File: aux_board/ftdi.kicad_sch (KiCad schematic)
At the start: 12 parts, among them U4 FT230XS

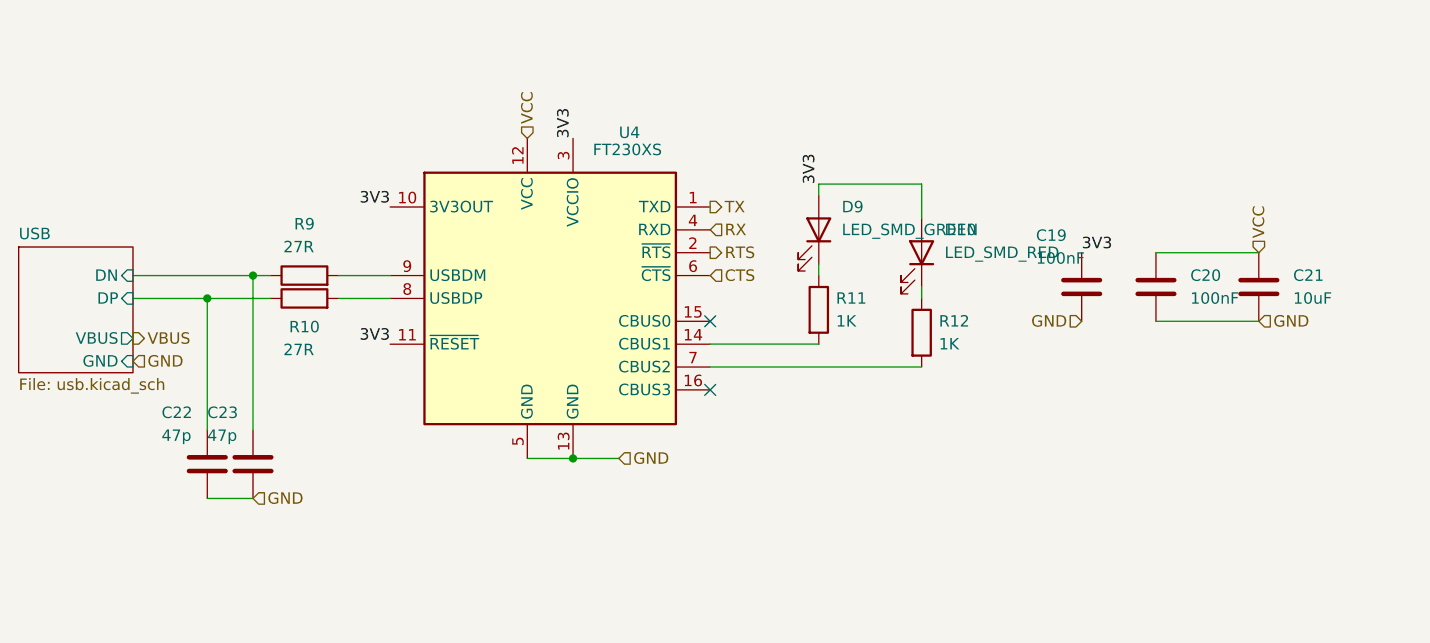
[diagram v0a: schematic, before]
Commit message: tweaking SCI and AUX for production, using common sheets as much as possible
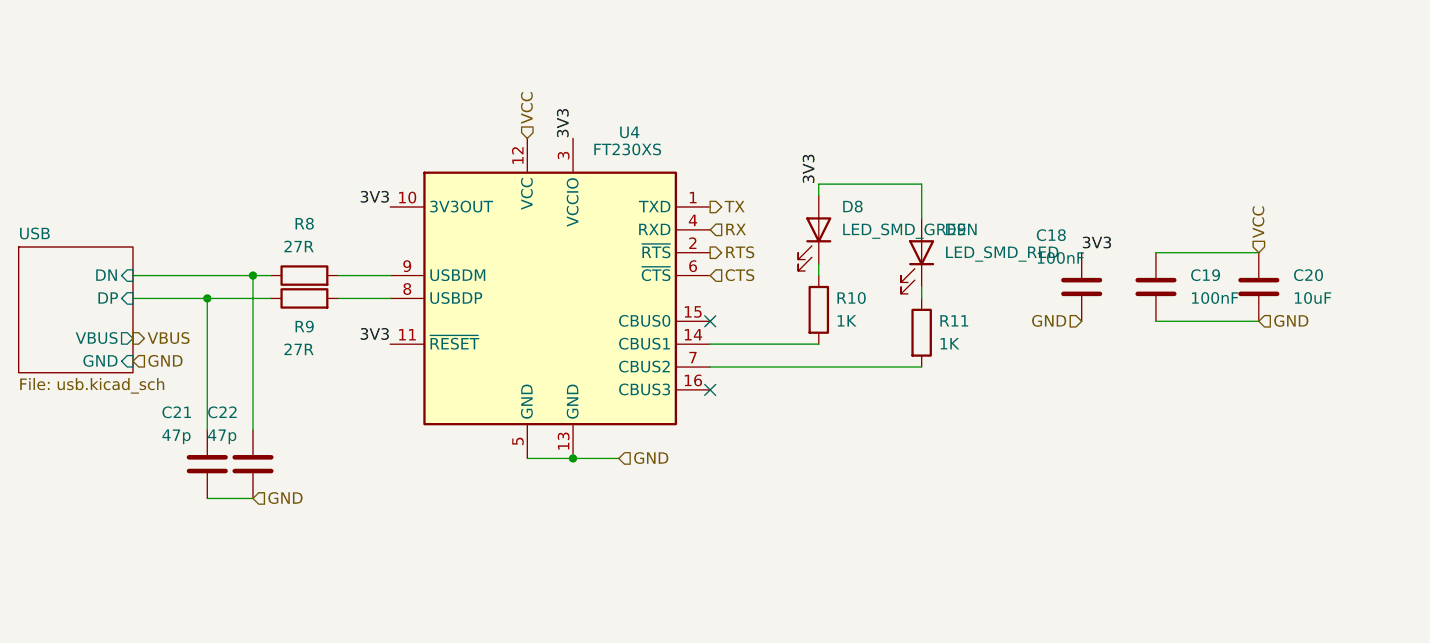
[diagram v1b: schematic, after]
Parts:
- renumbered C19 to C18, C20 to C19, C21 to C20, C22 to C21, C23 to C22, D9 to D8, D10 to D9, R11 to R10, R12 to R11, R9 to R8, R10 to R9
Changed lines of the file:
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@@
 		(on_board yes)
 		(dnp no)
-		(property "Reference" "D9"
+		(property "Reference" "D8"
 			(at 173.355 79.375 90)
 			(effects
@@
 			(project "aux_board"
 				(path "/85134265-2435-454a-99c4-e49d8e69c5c2/490a0c5b-9225-4953-ad7a-fe6abb29cde0/5590b01a-e5bf-4b57-b49e-9bcea37f7d3d"
-					(reference "D9")
+					(reference "D8")
 					(unit 1)
 				)
 				(path "/85134265-2435-454a-99c4-e49d8e69c5c2/490a0c5b-9225-4953-ad7a-fe6abb29cde0/d0d594aa-f069-4758-ae70-ed6ba42e7e43"
-					(reference "D11")
+					(reference "D10")
 					(unit 1)
 				)
@@
 		(dnp no)
 		(fields_autoplaced yes)
-		(property "Reference" "C21"
+		(property "Reference" "C20"
 			(at 223.52 86.9949 0)
 			(effects
@@
 			(project "aux_board"
 				(path "/85134265-2435-454a-99c4-e49d8e69c5c2/490a0c5b-9225-4953-ad7a-fe6abb29cde0/5590b01a-e5bf-4b57-b49e-9bcea37f7d3d"
-					(reference "C21")
+					(reference "C20")
 					(unit 1)
 				)
 				(path "/85134265-2435-454a-99c4-e49d8e69c5c2/490a0c5b-9225-4953-ad7a-fe6abb29cde0/d0d594aa-f069-4758-ae70-ed6ba42e7e43"
-					(reference "C26")
+					(reference "C25")
 					(unit 1)
 				)
@@
 		(on_board yes)
 		(dnp no)
-		(property "Reference" "D10"
+		(property "Reference" "D9"
 			(at 184.785 81.915 90)
 			(effects
@@
 			(project "aux_board"
 				(path "/85134265-2435-454a-99c4-e49d8e69c5c2/490a0c5b-9225-4953-ad7a-fe6abb29cde0/5590b01a-e5bf-4b57-b49e-9bcea37f7d3d"
-					(reference "D10")
+					(reference "D9")
 					(unit 1)
 				)
 				(path "/85134265-2435-454a-99c4-e49d8e69c5c2/490a0c5b-9225-4953-ad7a-fe6abb29cde0/d0d594aa-f069-4758-ae70-ed6ba42e7e43"
-					(reference "D12")
+					(reference "D11")
 					(unit 1)
 				)
@@
 		(dnp no)
 		(fields_autoplaced yes)
-		(property "Reference" "R11"
+		(property "Reference" "R10"
 			(at 172.72 89.5349 0)
 			(effects
@@
 			(project "aux_board"
 				(path "/85134265-2435-454a-99c4-e49d8e69c5c2/490a0c5b-9225-4953-ad7a-fe6abb29cde0/5590b01a-e5bf-4b57-b49e-9bcea37f7d3d"
-					(reference "R11")
+					(reference "R10")
 					(unit 1)
 				)
 				(path "/85134265-2435-454a-99c4-e49d8e69c5c2/490a0c5b-9225-4953-ad7a-fe6abb29cde0/d0d594aa-f069-4758-ae70-ed6ba42e7e43"
-					(reference "R17")
+					(reference "R16")
 					(unit 1)
 				)
@@
 		(on_board yes)
 		(dnp no)
-		(property "Reference" "C23"
+		(property "Reference" "C22"
 			(at 102.87 102.235 0)
 			(effects
@@
 			(project "aux_board"
 				(path "/85134265-2435-454a-99c4-e49d8e69c5c2/490a0c5b-9225-4953-ad7a-fe6abb29cde0/5590b01a-e5bf-4b57-b49e-9bcea37f7d3d"
-					(reference "C23")
+					(reference "C22")
 					(unit 1)
 				)
 				(path "/85134265-2435-454a-99c4-e49d8e69c5c2/490a0c5b-9225-4953-ad7a-fe6abb29cde0/d0d594aa-f069-4758-ae70-ed6ba42e7e43"
-					(reference "C28")
+					(reference "C27")
 					(unit 1)
 				)
@@
 		(dnp no)
 		(fields_autoplaced yes)
-		(property "Reference" "R12"
+		(property "Reference" "R11"
 			(at 184.15 92.0749 0)
 			(effects
@@
 			(project "aux_board"
 				(path "/85134265-2435-454a-99c4-e49d8e69c5c2/490a0c5b-9225-4953-ad7a-fe6abb29cde0/5590b01a-e5bf-4b57-b49e-9bcea37f7d3d"
-					(reference "R12")
+					(reference "R11")
 					(unit 1)
 				)
 				(path "/85134265-2435-454a-99c4-e49d8e69c5c2/490a0c5b-9225-4953-ad7a-fe6abb29cde0/d0d594aa-f069-4758-ae70-ed6ba42e7e43"
-					(reference "R18")
+					(reference "R17")
 					(unit 1)
 				)
@@
 		(on_board yes)
 		(dnp no)
-		(property "Reference" "R9"
+		(property "Reference" "R8"
 			(at 113.665 81.28 90)
 			(effects
@@
 			(project ""
 				(path "/85134265-2435-454a-99c4-e49d8e69c5c2/490a0c5b-9225-4953-ad7a-fe6abb29cde0/5590b01a-e5bf-4b57-b49e-9bcea37f7d3d"
-					(reference "R9")
+					(reference "R8")
 					(unit 1)
 				)
 				(path "/85134265-2435-454a-99c4-e49d8e69c5c2/490a0c5b-9225-4953-ad7a-fe6abb29cde0/d0d594aa-f069-4758-ae70-ed6ba42e7e43"
-					(reference "R15")
+					(reference "R14")
 					(unit 1)
 				)
@@
 		(on_board yes)
 		(dnp no)
-		(property "Reference" "C19"
+		(property "Reference" "C18"
 			(at 194.945 82.55 0)
 			(effects
@@
 			(project "aux_board"
 				(path "/85134265-2435-454a-99c4-e49d8e69c5c2/490a0c5b-9225-4953-ad7a-fe6abb29cde0/5590b01a-e5bf-4b57-b49e-9bcea37f7d3d"
-					(reference "C19")
+					(reference "C18")
 					(unit 1)
 				)
 				(path "/85134265-2435-454a-99c4-e49d8e69c5c2/490a0c5b-9225-4953-ad7a-fe6abb29cde0/d0d594aa-f069-4758-ae70-ed6ba42e7e43"
-					(reference "C24")
+					(reference "C23")
 					(unit 1)
 				)
@@
 		(on_board yes)
 		(dnp no)
-		(property "Reference" "C22"
+		(property "Reference" "C21"
 			(at 97.79 102.235 0)
 			(effects
@@
 			(project "aux_board"
 				(path "/85134265-2435-454a-99c4-e49d8e69c5c2/490a0c5b-9225-4953-ad7a-fe6abb29cde0/5590b01a-e5bf-4b57-b49e-9bcea37f7d3d"
-					(reference "C22")
+					(reference "C21")
 					(unit 1)
 				)
 				(path "/85134265-2435-454a-99c4-e49d8e69c5c2/490a0c5b-9225-4953-ad7a-fe6abb29cde0/d0d594aa-f069-4758-ae70-ed6ba42e7e43"
-					(reference "C27")
+					(reference "C26")
 					(unit 1)
 				)
@@
 		(dnp no)
 		(fields_autoplaced yes)
-		(property "Reference" "C20"
+		(property "Reference" "C19"
 			(at 212.09 86.9949 0)
 			(effects
@@
 			(project ""
 				(path "/85134265-2435-454a-99c4-e49d8e69c5c2/490a0c5b-9225-4953-ad7a-fe6abb29cde0/5590b01a-e5bf-4b57-b49e-9bcea37f7d3d"
-					(reference "C20")
+					(reference "C19")
 					(unit 1)
 				)
 				(path "/85134265-2435-454a-99c4-e49d8e69c5c2/490a0c5b-9225-4953-ad7a-fe6abb29cde0/d0d594aa-f069-4758-ae70-ed6ba42e7e43"
-					(reference "C25")
+					(reference "C24")
 					(unit 1)
 				)
@@
 		(on_board yes)
 		(dnp no)
-		(property "Reference" "R10"
+		(property "Reference" "R9"
 			(at 113.665 92.71 90)
 			(effects
@@
 			(project "aux_board"
 				(path "/85134265-2435-454a-99c4-e49d8e69c5c2/490a0c5b-9225-4953-ad7a-fe6abb29cde0/5590b01a-e5bf-4b57-b49e-9bcea37f7d3d"
-					(reference "R10")
+					(reference "R9")
 					(unit 1)
 				)
 				(path "/85134265-2435-454a-99c4-e49d8e69c5c2/490a0c5b-9225-4953-ad7a-fe6abb29cde0/d0d594aa-f069-4758-ae70-ed6ba42e7e43"
-					(reference "R16")
-					(unit 1)
-				)
+					(reference "R15")
+					(unit 1)
+				)

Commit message: clenup BOM for SCI and AUX
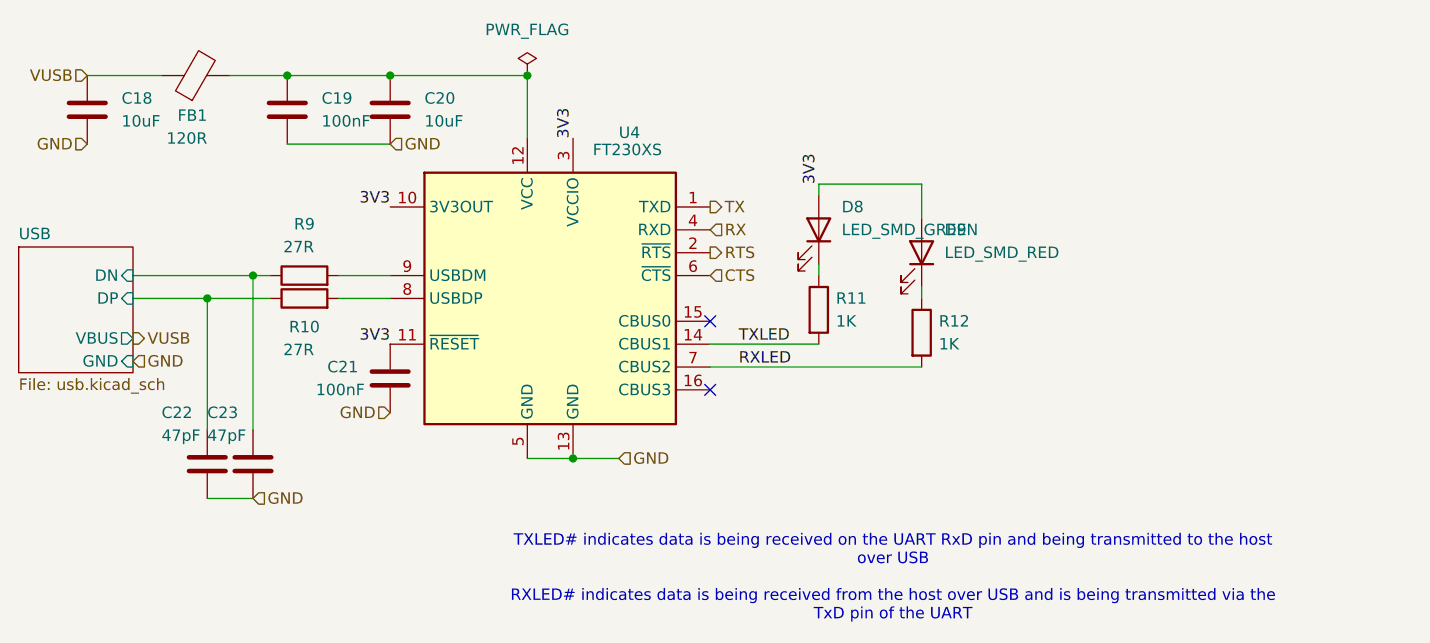
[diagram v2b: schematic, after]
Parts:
- added C18: 10uF, Capacitor_SMD:C_0603_1608Metric_Pad1.08x0.95mm_HandSolder, symbol Device:C
- added FB1: 120R, Inductor_SMD:L_0603_1608Metric_Pad1.05x0.95mm_HandSolder, symbol Device:FerriteBead
- C22: renamed from C21; value 47p -> 47pF
- C23: renamed from C22; value 47p -> 47pF
- R10: renamed from R9; Part Number RC0603JR-0727RL -> RC0603FR-0727RL
- R9: renamed from R8; Part Number RC0603JR-0727RL -> RC0603FR-0727RL
- renumbered C18 to C21, R10 to R11, R11 to R12
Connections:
- net GND: now also C18.2
- net TXLED: now reaches R11.2, U4.14 (CBUS1)
- net RXLED: now reaches R12.2, U4.7 (CBUS2)
- net VCC: no longer names the net of C19.1, C20.1, U4.12 (VCC)
- net VCC: now also FB1.2
- new net VUSB: C18.1, FB1.1
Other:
- note added: "TXLED# indicates data is being received on the UART RxD pin and being transmitted to the host over USB RXLED# indicates data is being received from the host over USB and is being transmitted via the TxD pin of the UART"
- moved on the sheet: C19, C20, C21

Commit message: QC, add second 3V regulator to AUX, INT pullups on AUX SCI AVI
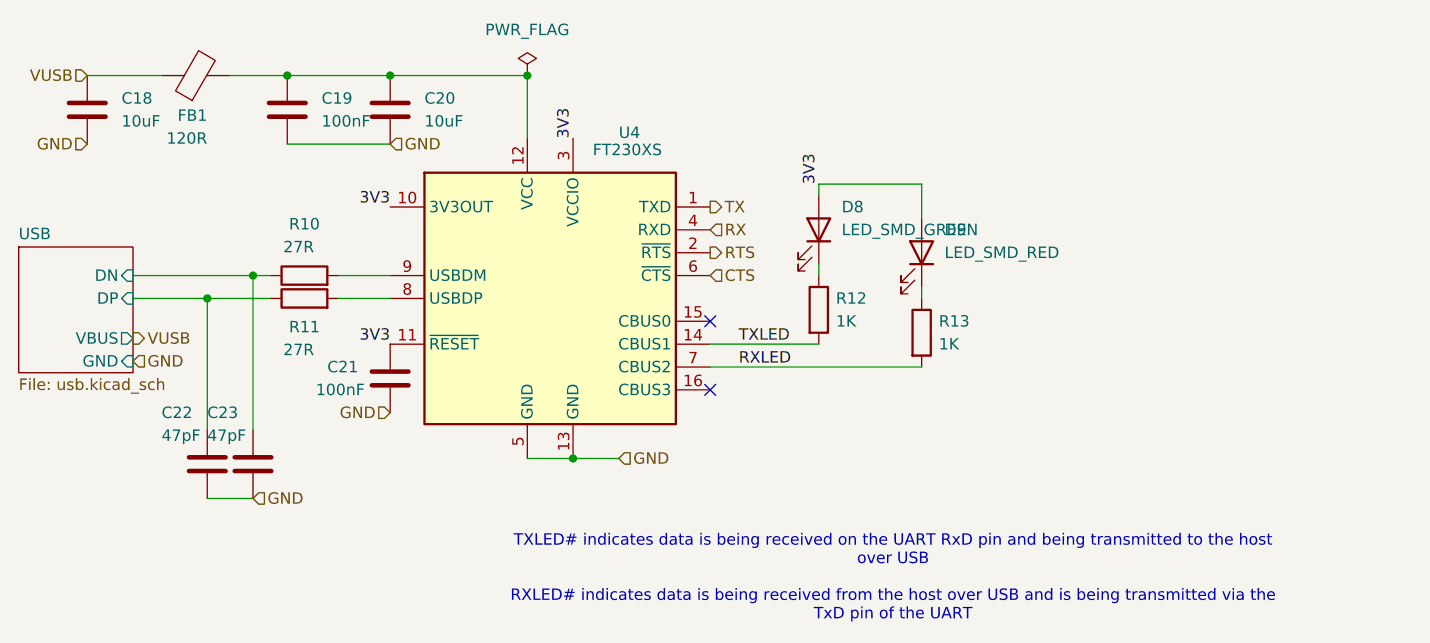
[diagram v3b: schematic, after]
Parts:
- renumbered R9 to R10, R10 to R11, R11 to R12, R12 to R13
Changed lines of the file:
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@@
 		(dnp no)
 		(fields_autoplaced yes)
-		(property "Reference" "R11"
+		(property "Reference" "R12"
 			(at 172.72 89.5349 0)
 			(effects
@@
 			(project "aux_board"
 				(path "/85134265-2435-454a-99c4-e49d8e69c5c2/490a0c5b-9225-4953-ad7a-fe6abb29cde0/5590b01a-e5bf-4b57-b49e-9bcea37f7d3d"
-					(reference "R11")
+					(reference "R12")
 					(unit 1)
 				)
 				(path "/85134265-2435-454a-99c4-e49d8e69c5c2/490a0c5b-9225-4953-ad7a-fe6abb29cde0/d0d594aa-f069-4758-ae70-ed6ba42e7e43"
-					(reference "R17")
+					(reference "R18")
 					(unit 1)
 				)
@@
 		(dnp no)
 		(fields_autoplaced yes)
-		(property "Reference" "R12"
+		(property "Reference" "R13"
 			(at 184.15 92.0749 0)
 			(effects
@@
 			(project "aux_board"
 				(path "/85134265-2435-454a-99c4-e49d8e69c5c2/490a0c5b-9225-4953-ad7a-fe6abb29cde0/5590b01a-e5bf-4b57-b49e-9bcea37f7d3d"
-					(reference "R12")
+					(reference "R13")
 					(unit 1)
 				)
 				(path "/85134265-2435-454a-99c4-e49d8e69c5c2/490a0c5b-9225-4953-ad7a-fe6abb29cde0/d0d594aa-f069-4758-ae70-ed6ba42e7e43"
-					(reference "R18")
+					(reference "R19")
 					(unit 1)
 				)
@@
 		(on_board yes)
 		(dnp no)
-		(property "Reference" "R9"
+		(property "Reference" "R10"
 			(at 113.665 81.28 90)
 			(effects
@@
 			(project ""
 				(path "/85134265-2435-454a-99c4-e49d8e69c5c2/490a0c5b-9225-4953-ad7a-fe6abb29cde0/5590b01a-e5bf-4b57-b49e-9bcea37f7d3d"
-					(reference "R9")
+					(reference "R10")
 					(unit 1)
 				)
 				(path "/85134265-2435-454a-99c4-e49d8e69c5c2/490a0c5b-9225-4953-ad7a-fe6abb29cde0/d0d594aa-f069-4758-ae70-ed6ba42e7e43"
-					(reference "R15")
+					(reference "R16")
 					(unit 1)
 				)
@@
 		(on_board yes)
 		(dnp no)
-		(property "Reference" "R10"
+		(property "Reference" "R11"
 			(at 113.665 92.71 90)
 			(effects
@@
 			(project "aux_board"
 				(path "/85134265-2435-454a-99c4-e49d8e69c5c2/490a0c5b-9225-4953-ad7a-fe6abb29cde0/5590b01a-e5bf-4b57-b49e-9bcea37f7d3d"
-					(reference "R10")
+					(reference "R11")
 					(unit 1)
 				)
 				(path "/85134265-2435-454a-99c4-e49d8e69c5c2/490a0c5b-9225-4953-ad7a-fe6abb29cde0/d0d594aa-f069-4758-ae70-ed6ba42e7e43"
-					(reference "R16")
-					(unit 1)
-				)
+					(reference "R17")
+					(unit 1)
+				)

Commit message: propate the changes to RF
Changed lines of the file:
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@@
 		)
 		(property "Value" "LED_SMD_GREEN"
-			(at 173.355 81.915 90)
+			(at 172.72 77.47 90)
 			(effects
 				(font
@@
 		)
 		(property "Voltage" "2"
-			(at 170.815 81.915 0)
-			(effects
-				(font
-					(size 1.27 1.27)
-				)
-				(hide yes)
-			)
-		)
-		(property "PARTREV" ""
-			(at 170.815 81.915 0)
-			(effects
-				(font
-					(size 1.27 1.27)
-				)
-				(hide yes)
-			)
-		)
-		(property "STANDARD" ""
 			(at 170.815 81.915 0)
 			(effects
@@
 			)
 		)
-		(property "PARTREV" ""
-			(at 123.19 68.58 0)
-			(effects
-				(font
-					(size 1.27 1.27)
-				)
-				(hide yes)
-			)
-		)
-		(property "STANDARD" ""
-			(at 123.19 68.58 0)
-			(effects
-				(font
-					(size 1.27 1.27)
-				)
-				(hide yes)
-			)
-		)
 		(pin "1"
 		)
@@
 		(dnp no)
 		(property "Reference" "D9"
-			(at 184.785 81.915 90)
+			(at 185.42 86.36 90)
 			(effects
 				(font
@@
 		)
 		(property "Voltage" "2"
-			(at 182.245 84.455 0)
-			(effects
-				(font
-					(size 1.27 1.27)
-				)
-				(hide yes)
-			)
-		)
-		(property "PARTREV" ""
-			(at 182.245 84.455 0)
-			(effects
-				(font
-					(size 1.27 1.27)
-				)
-				(hide yes)
-			)
-		)
-		(property "STANDARD" ""
 			(at 182.245 84.455 0)
 			(effects
@@
 			)
 		)
-		(property "PARTREV" ""
-			(at 170.815 90.805 0)
-			(effects
-				(font
-					(size 1.27 1.27)
-				)
-				(hide yes)
-			)
-		)
-		(property "STANDARD" ""
-			(at 170.815 90.805 0)
-			(effects
-				(font
-					(size 1.27 1.27)
-				)
-				(hide yes)
-			)
-		)
 		(pin "2"
 		)
@@
 			)
 		)
-		(property "PARTREV" ""
-			(at 140.97 89.535 0)
-			(effects
-				(font
-					(size 1.27 1.27)
-				)
-				(hide yes)
-			)
-		)
-		(property "STANDARD" ""
-			(at 140.97 89.535 0)
-			(effects
-				(font
-					(size 1.27 1.27)
-				)
-				(hide yes)
-			)
-		)
 		(pin "4"
 		)
@@
 		)
 		(property "Voltage" "50"
-			(at 107.95 107.95 0)
-			(effects
-				(font
-					(size 1.27 1.27)
-				)
-				(hide yes)
-			)
-		)
-		(property "PARTREV" ""
-			(at 107.95 107.95 0)
-			(effects
-				(font
-					(size 1.27 1.27)
-				)
-				(hide yes)
-			)
-		)
-		(property "STANDARD" ""
 			(at 107.95 107.95 0)
 			(effects
@@
 			)
 		)
-		(property "PARTREV" ""
-			(at 182.245 93.345 0)
-			(effects
-				(font
-					(size 1.27 1.27)
-				)
-				(hide yes)
-			)
-		)
-		(property "STANDARD" ""
-			(at 182.245 93.345 0)
-			(effects
-				(font
-					(size 1.27 1.27)
-				)
-				(hide yes)
-			)
-		)
 		(pin "2"
 		)
@@
 			)
 		)
-		(property "PARTREV" ""
-			(at 113.665 86.995 0)
-			(effects
-				(font
-					(size 1.27 1.27)
-				)
-				(hide yes)
-			)
-		)
-		(property "STANDARD" ""
-			(at 113.665 86.995 0)
-			(effects
-				(font
-					(size 1.27 1.27)
-				)
-				(hide yes)
-			)
-		)
 		(pin "1"
 		)
@@
 			)
 		)
-		(property "PARTREV" ""
-			(at 123.19 98.425 0)
-			(effects
-				(font
-					(size 1.27 1.27)
-				)
-				(hide yes)
-			)
-		)
-		(property "STANDARD" ""
-			(at 123.19 98.425 0)
-			(effects
-				(font
-					(size 1.27 1.27)
-				)
-				(hide yes)
-			)
-		)
 		(pin "1"
 		)
@@
 		)
 		(property "Voltage" "50"
-			(at 102.87 107.95 0)
-			(effects
-				(font
-					(size 1.27 1.27)
-				)
-				(hide yes)
-			)
-		)
-		(property "PARTREV" ""
-			(at 102.87 107.95 0)
-			(effects
-				(font
-					(size 1.27 1.27)
-				)
-				(hide yes)
-			)
-		)
-		(property "STANDARD" ""
 			(at 102.87 107.95 0)
 			(effects
@@
 			)
 		)
-		(property "PARTREV" ""
-			(at 111.76 68.58 0)
-			(effects
-				(font
-					(size 1.27 1.27)
-				)
-				(hide yes)
-			)
-		)
-		(property "STANDARD" ""
-			(at 111.76 68.58 0)
-			(effects
-				(font
-					(size 1.27 1.27)
-				)
-				(hide yes)
-			)
-		)
 		(pin "1"
 		)
@@
 			)
 		)
-		(property "PARTREV" ""
-			(at 89.535 68.58 0)
-			(effects
-				(font
-					(size 1.27 1.27)
-				)
-				(hide yes)
-			)
-		)
-		(property "STANDARD" ""
-			(at 89.535 68.58 0)
-			(effects
-				(font
-					(size 1.27 1.27)
-				)
-				(hide yes)
-			)
-		)
 		(pin "1"
 		)
@@
 			(at 113.665 89.535 0)
 			(effects
-				(font
-					(size 1.27 1.27)
-				)
-				(hide yes)
-			)
-		)
-		(property "PARTREV" ""
-			(at 113.665 89.535 0)
-			(effects
-				(font
-					(size 1.27 1.27)
-				)
-				(hide yes)
-			)
-		)
-		(property "STANDARD" ""
-			(at 113.665 89.535 0)
-			(effects
